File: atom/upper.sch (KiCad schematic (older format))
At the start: 20 parts, among them J101 MALE, J1010 MALE, J102 FEMALE, J103 MALE, J1030 MALE, J104 FEMALE, J105 MALE, J1050 MALE, J106 FEMALE, J107 MALE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

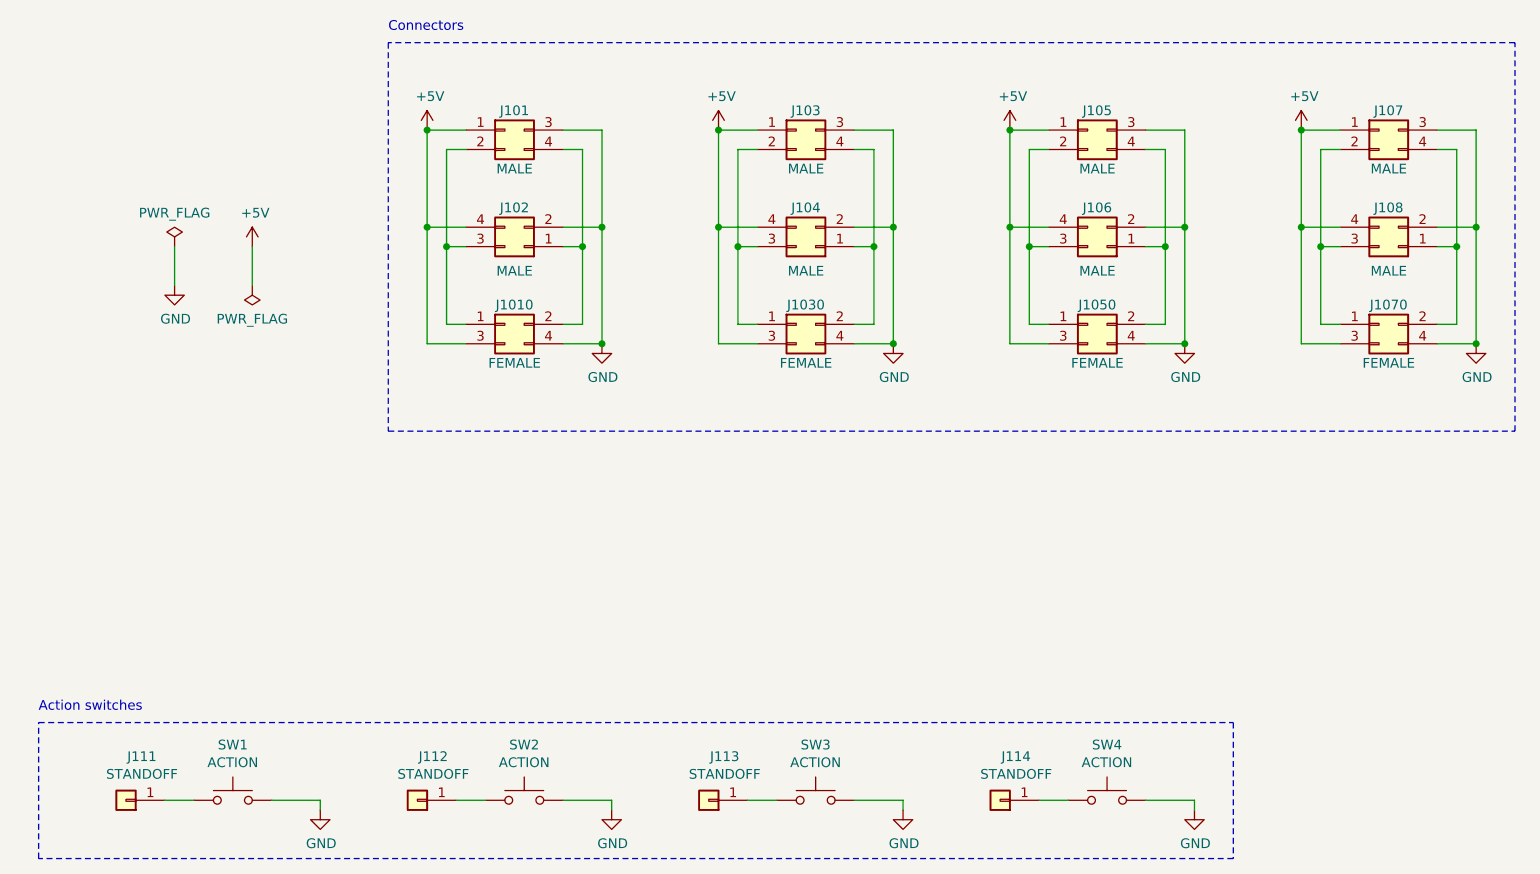
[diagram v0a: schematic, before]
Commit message: Fix: RX needs to be connected to TX
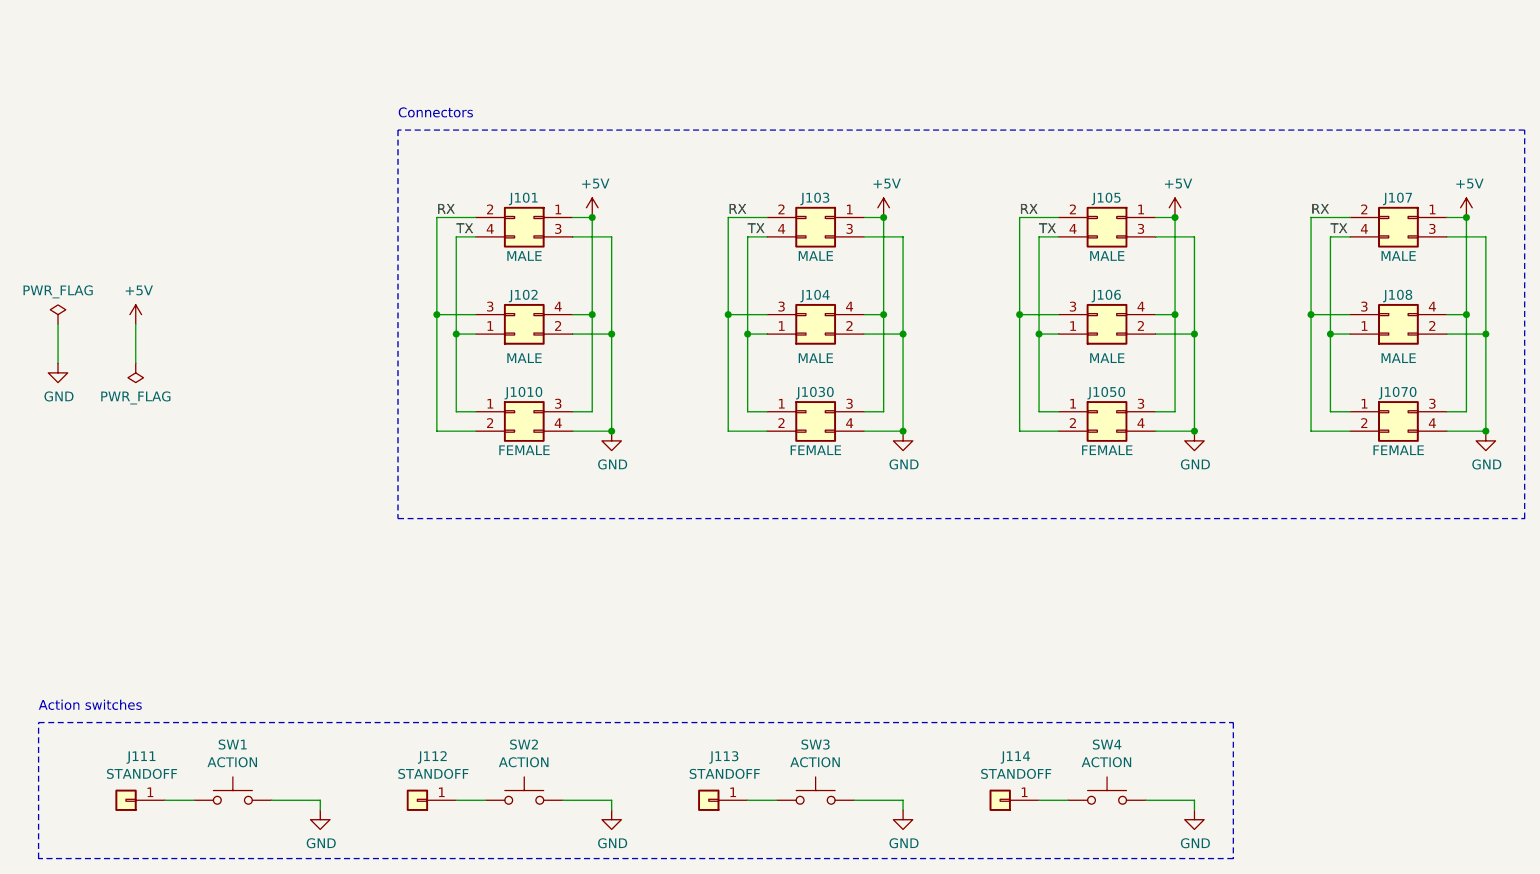
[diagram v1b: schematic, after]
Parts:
- removed J101, J1010, J103, J1030, J105, J1050, J107, J1070: MALE, Connector_PinHeader_2.54mm:PinHeader_2x02_P2.54mm_Horizontal, symbol Connector_Generic:Conn_02x02_Top_Bottom
- removed J102, J104, J106, J108: FEMALE, Connector_PinSocket_2.54mm:PinSocket_2x02_P2.54mm_Horizontal, symbol Connector_Generic:Conn_02x02_Odd_Even
- added J101, J1010, J103, J1030, J105, J1050, J107, J1070: MALE, Connector_PinHeader_2.54mm:PinHeader_2x02_P2.54mm_Horizontal, symbol Connector_Generic:Conn_02x02_Odd_Even
- added J102, J104, J106, J108: FEMALE, Connector_PinSocket_2.54mm:PinSocket_2x02_P2.54mm_Horizontal, symbol Connector_Generic:Conn_02x02_Top_Bottom
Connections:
- net +5V: now also J101.1 (Pin_1), J1010.4 (Pin_4), J102.3 (Pin_3), J103.1 (Pin_1), J1030.4 (Pin_4), J104.3 (Pin_3), J105.1 (Pin_1), J1050.4 (Pin_4), J106.3 (Pin_3), J107.1 (Pin_1), J1070.4 (Pin_4), J108.3 (Pin_3)
- net GND: now also J101.3 (Pin_3), J1010.2 (Pin_2), J102.4 (Pin_4), J103.3 (Pin_3), J1030.2 (Pin_2), J104.4 (Pin_4), J105.3 (Pin_3), J1050.2 (Pin_2), J106.4 (Pin_4), J107.3 (Pin_3), J1070.2 (Pin_2), J108.4 (Pin_4)
- new net RX: J101.2 (Pin_2), J1010.3 (Pin_3), J102.2 (Pin_2), J103.2 (Pin_2), J1030.3 (Pin_3), J104.2 (Pin_2), J105.2 (Pin_2), J1050.3 (Pin_3), J106.2 (Pin_2), J107.2 (Pin_2), J1070.3 (Pin_3), J108.2 (Pin_2)
- new net TX: J101.4 (Pin_4), J1010.1 (Pin_1), J102.1 (Pin_1), J103.4 (Pin_4), J1030.1 (Pin_1), J104.1 (Pin_1), J105.4 (Pin_4), J1050.1 (Pin_1), J106.1 (Pin_1), J107.4 (Pin_4), J1070.1 (Pin_1), J108.1 (Pin_1)

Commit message: Preserve Unique IDs of connectors
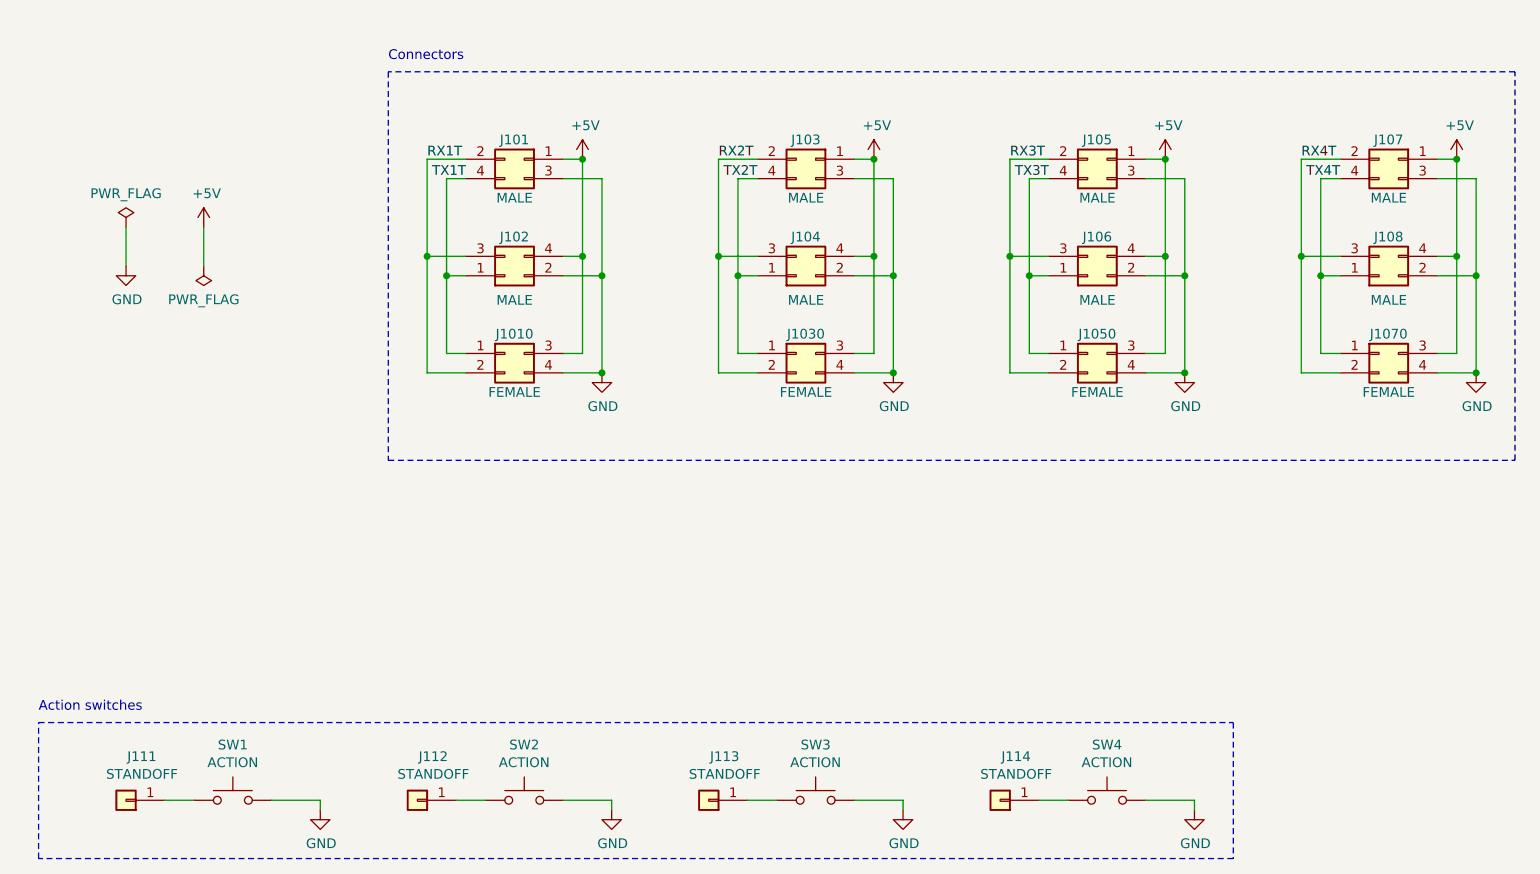
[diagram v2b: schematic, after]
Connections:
- removed net RX: J101.2 (Pin_2), J1010.3 (Pin_3), J102.2 (Pin_2), J103.2 (Pin_2), J1030.3 (Pin_3), J104.2 (Pin_2), J105.2 (Pin_2), J1050.3 (Pin_3), J106.2 (Pin_2), J107.2 (Pin_2), J1070.3 (Pin_3), J108.2 (Pin_2)
- removed net TX: J101.4 (Pin_4), J1010.1 (Pin_1), J102.1 (Pin_1), J103.4 (Pin_4), J1030.1 (Pin_1), J104.1 (Pin_1), J105.4 (Pin_4), J1050.1 (Pin_1), J106.1 (Pin_1), J107.4 (Pin_4), J1070.1 (Pin_1), J108.1 (Pin_1)
- new net RX1T: J101.2 (Pin_2), J1010.3 (Pin_3), J102.2 (Pin_2)
- new net RX2T: J103.2 (Pin_2), J1030.3 (Pin_3), J104.2 (Pin_2)
- new net RX3T: J105.2 (Pin_2), J1050.3 (Pin_3), J106.2 (Pin_2)
- new net RX4T: J107.2 (Pin_2), J1070.3 (Pin_3), J108.2 (Pin_2)
- new net TX1T: J101.4 (Pin_4), J1010.1 (Pin_1), J102.1 (Pin_1)
- new net TX2T: J103.4 (Pin_4), J1030.1 (Pin_1), J104.1 (Pin_1)
- new net TX3T: J105.4 (Pin_4), J1050.1 (Pin_1), J106.1 (Pin_1)
- new net TX4T: J107.4 (Pin_4), J1070.1 (Pin_1), J108.1 (Pin_1)
